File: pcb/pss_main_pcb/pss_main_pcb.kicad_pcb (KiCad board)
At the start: 2 copper layers, 177.8 x 55.9 mm, 96 parts, among them J1 24V DC Input, J2 220V AC Input, J3 Hot Air Gun, J4 Soldering Iron, J5 STM32_Prog, J6 UART_Prog, Q1 BC817, Q2 MMBT2222, Q3 MMBT2907, Q4 IRLML9301T, Q5 IRFZ44S, Q6 BT139B-800, SW1 Hot Air Gun Input, SW2 Soldering Iron Input, SW3 SW_Push, SW4 Main Encoder Input, SW5 EN, SW6 Boot, U1 LM2596S-5, U2 LM2596S-3.3, U3 MOC3023S, U4 LM358, U5 STM32F030K6Tx, U6 ESP32-WROOM-32U, U7 2.8inch_SPI_Module_ILI9341_SK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

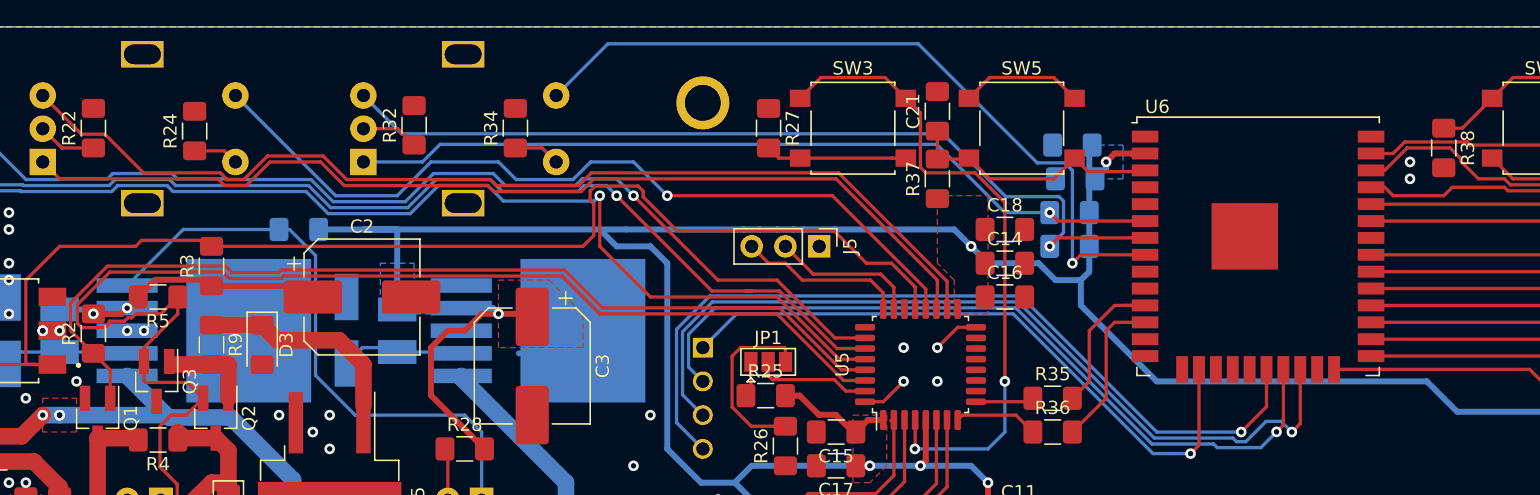
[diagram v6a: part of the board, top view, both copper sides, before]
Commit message: Change components placement and routes
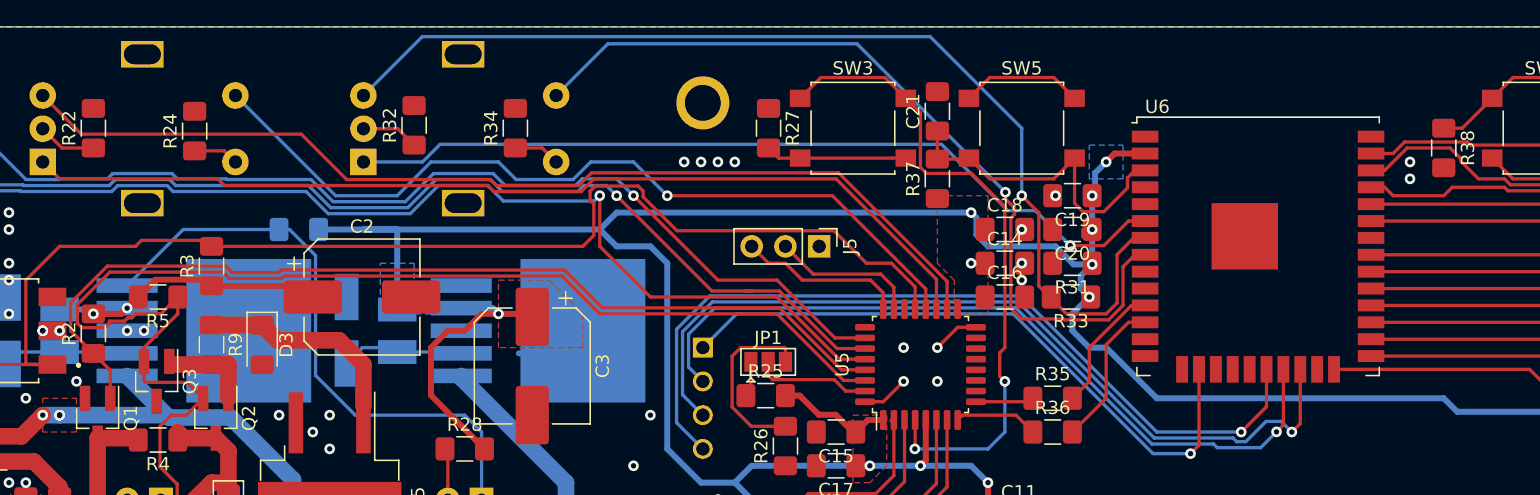
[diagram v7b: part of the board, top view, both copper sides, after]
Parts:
- C19, C20, R31, R33: moved to F.Cu
- moved C20 3.82 mm to (180.3, 77.5)
- moved R31 3.82 mm to (180.3, 80.0)
- moved R33 3.81 mm to (180.2, 82.5)
- moved C19 3.81 mm to (180.3, 74.9)
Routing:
- net Main_Enc_B: track 67.2 -> 80.0 mm
- net Main_Switch: track 57.1 -> 63.4 mm
- net EN: track 19.3 -> 24.4 mm
- net Main_Enc_A: track 61.7 -> 65.2 mm
- net +3V3: track 285.6 -> 288.5 mm, vias 7 -> 12
- net ESP32_UART_TX: track 12.2 -> 9.85 mm
- net Sold_Enc_A: track 75.5 -> 73.9 mm
- net Sold_Enc_B: track 78.2 -> 76.7 mm
- net ESP32_UART_RX: track 11.9 -> 11.3 mm
- net GND: vias 54 -> 62

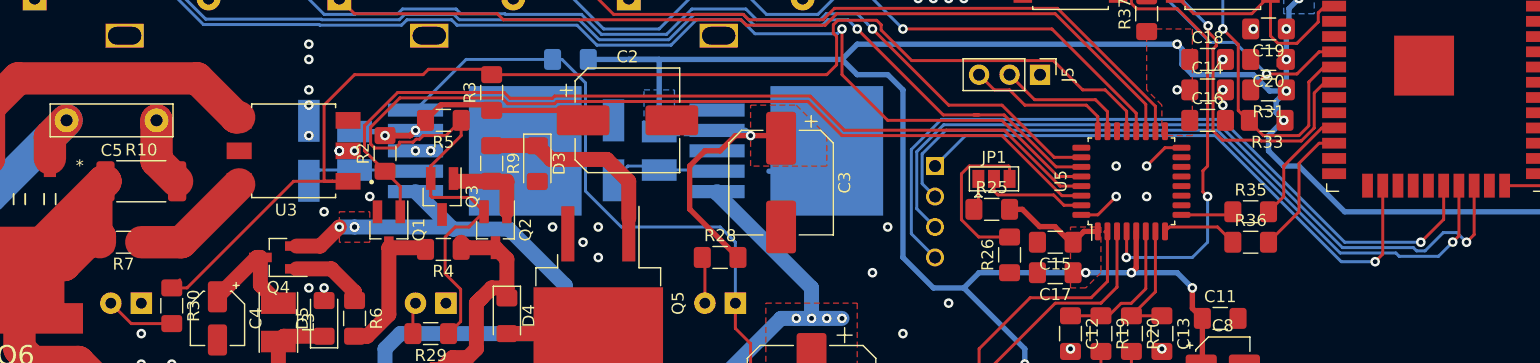
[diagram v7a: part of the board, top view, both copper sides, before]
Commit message: Add display 3D model for PCB design
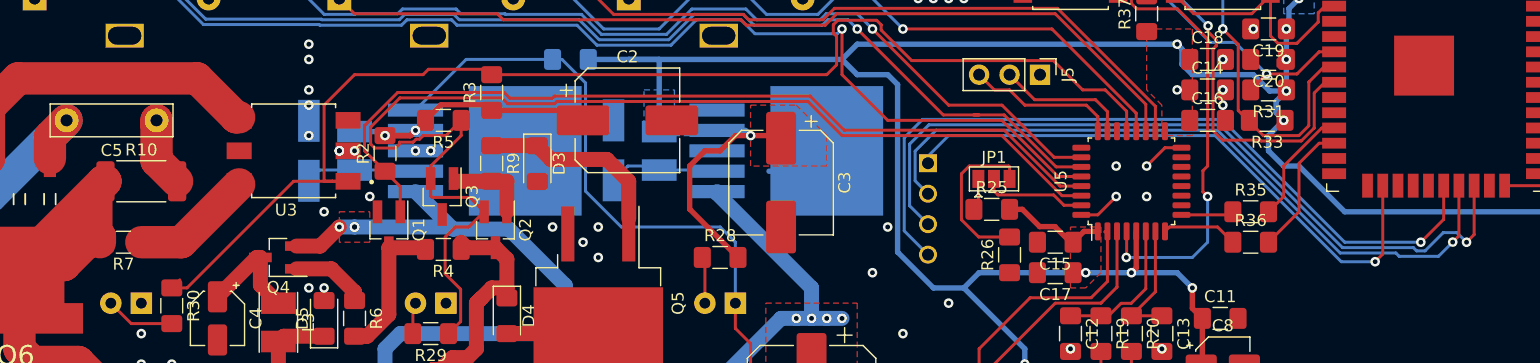
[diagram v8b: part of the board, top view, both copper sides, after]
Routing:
- net SD_SCK: track 63.1 -> 64.0 mm
- net SD_CS: track 48.7 -> 49.5 mm
- net SD_SDO: track 64.0 -> 64.7 mm
